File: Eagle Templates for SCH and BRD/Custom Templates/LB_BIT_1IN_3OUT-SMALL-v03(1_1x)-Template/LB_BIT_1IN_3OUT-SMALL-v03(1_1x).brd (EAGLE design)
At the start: 74.2 x 11.6 mm, 16 parts, among them U1 LV321SOT23-5

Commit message: added bitlab logo and made minor changes to board templates. Updated littlebits library.
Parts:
- added U$2: (no value), LITTLEBITS:BITLAB-LOGO
- moved U$8 4.30 mm to (67.3, 9.33)
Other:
- board text added: "iX Name Here"
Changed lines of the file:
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@@
 <layer number="113" name="extra" color="10" fill="1" visible="yes" active="yes"/>
 <layer number="116" name="Patch_BOT" color="7" fill="1" visible="yes" active="yes"/>
+<layer number="118" name="Rect_Pads" color="7" fill="1" visible="no" active="yes"/>
 <layer number="121" name="_tsilk" color="7" fill="1" visible="yes" active="yes"/>
 <layer number="122" name="_bsilk" color="7" fill="1" visible="yes" active="yes"/>
@@
 <wire x1="2.51" y1="12.705" x2="5.51" y2="15.705" width="1" layer="46" curve="-90"/>
 <wire x1="2.51" y1="4.11" x2="3.39" y2="4.11" width="1" layer="46"/>
+<text x="72.9" y="9.7" size="1.3" layer="21" font="vector" rot="SR270" align="center">iX Name
+Here</text>
 </plain>
 <attributes>
@@
 </autorouter>
 <elements>
-<element name="U$8" library="ohw-logo" package="OSHW_FILLX150_NOTEXT" value="" x="71.633" y="9.428"/>
+<element name="U$8" library="ohw-logo" package="OSHW_FILLX150_NOTEXT" value="" x="67.333" y="9.328"/>
 <element name="U1" library="LITTLEBITS" package="SOT23-5" value="LV321SOT23-5" x="42.125" y="10.465" rot="MR270"/>
 <element name="I?R1" library="LITTLEBITS" package="RES-0603" value="1meg" x="39.58" y="13.16" rot="MR180">
@@
 <element name="U$1" library="LITTLEBITS" package="OSHWCREDIT" value="OSHWCREDIT" x="-88.27" y="-63.05"/>
 <element name="FRAME1" library="LITTLEBITS" package="FABDWG01-OHW" value="FRAME-LETTER" x="0" y="0"/>
+<element name="U$2" library="LITTLEBITS" package="BITLAB-LOGO" value="" x="72" y="13.6" rot="R270"/>
 </elements>
 <signals>

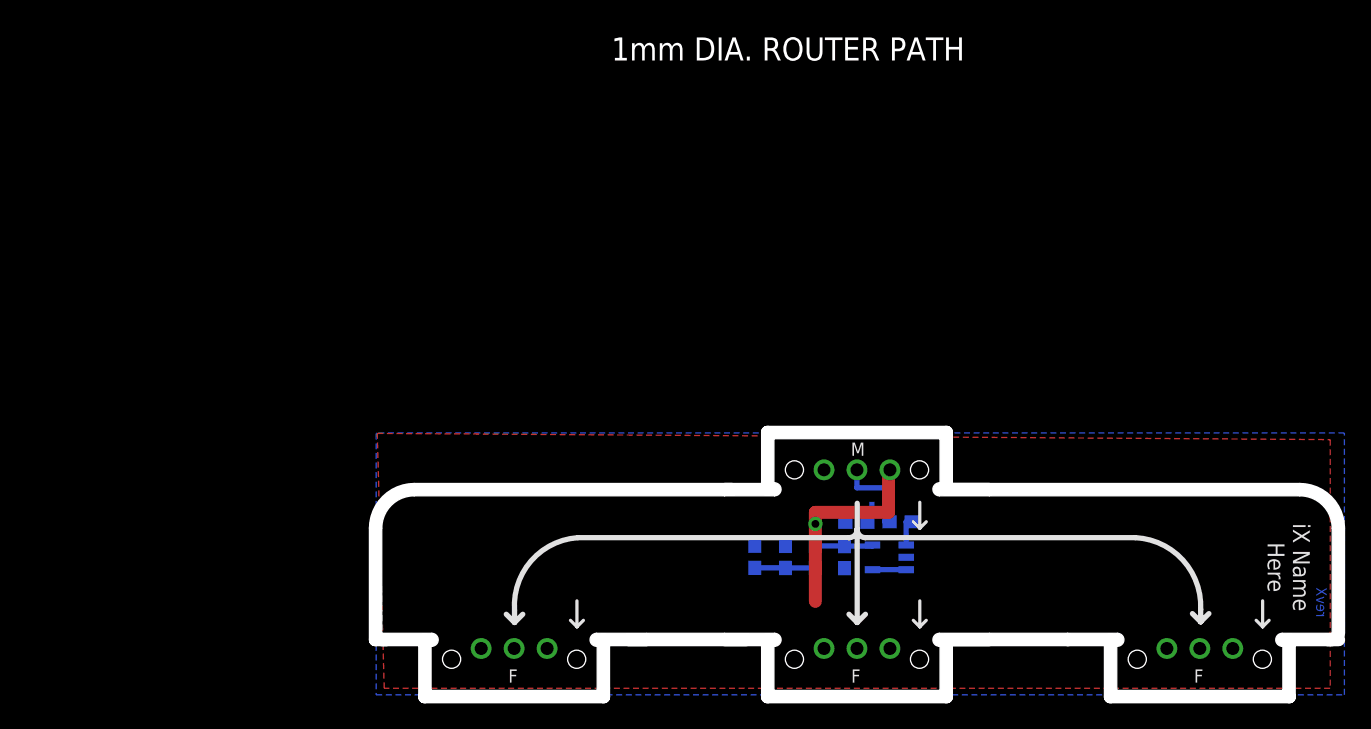
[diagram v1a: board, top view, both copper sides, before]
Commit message: Updated templates
- Added ferrite beads
- Moved text and annotations off of Nets layer
- Minor layout changes
- Removed I/O/W prefix from reference designators
- Removed output stage components from output bits
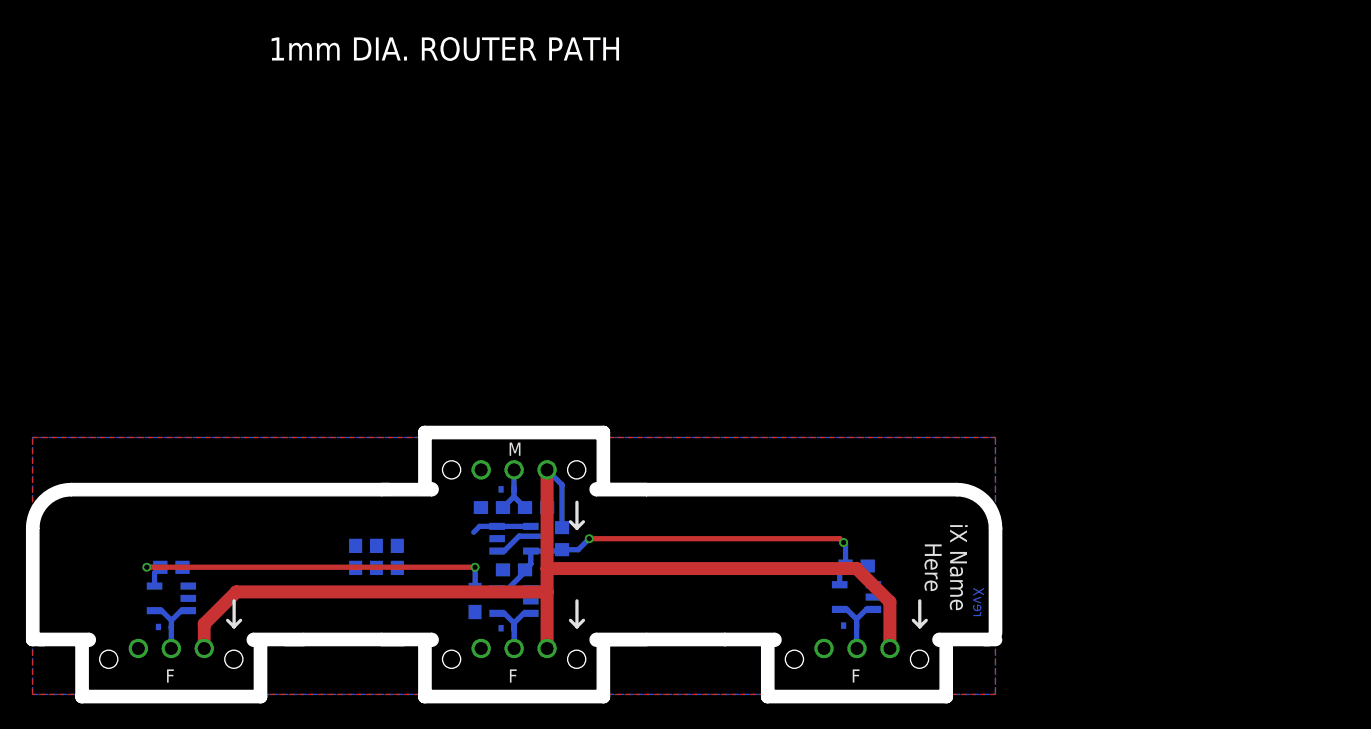
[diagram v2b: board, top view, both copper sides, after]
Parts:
- removed I?BSF2: BITSNAP_V03_FEMALE, bitSnap:BITSNAP_V03_FEMALE
- removed I?C1: 0.1uF, LITTLEBITS:CAP-0603
- removed I?C2: 10uF, LITTLEBITS:CAP-0603
- removed I?R1: 1meg, LITTLEBITS:RES-0603
- removed I?R2: 10K, LITTLEBITS:RES-0603
- removed I?R3, I?R4: 3K3, LITTLEBITS:RES-0603
- removed I?TVS1: ESD9B5.0ST5G, LITTLEBITS:SOD-923
- added BSF1: BITSNAP_V03_FEMALE, bitSnap:BITSNAP_V03_FEMALE
- added C1: 0.1uF, LITTLEBITS:CAP-0603
- added C2: 10uF, LITTLEBITS:CAP-0603
- added C3, C4, C5: 1.0uF, LITTLEBITS:CAP-0603
- added FB1: FERRITE-BEAD0603, LITTLEBITS:R0603
- added R1: 1meg, LITTLEBITS:RES-0603
- added R2: 10K, LITTLEBITS:RES-0603
- added R3, R4: 3K3, LITTLEBITS:RES-0603
- added TVS1, TVS2, TVS3, TVS4: ESD9B5.0ST5G, LITTLEBITS:SOD-923
- added U2, U3, U4: LV321SOT23-5, LITTLEBITS:SOT23-5
- moved U1 29.0 mm to (13.2, 11.9), turned to 90 degrees
- moved U$2 26.4 mm to (45.6, 13.6)
- moved U$8 26.4 mm to (40.9, 9.33)
- moved I?BSM 26.4 mm to (19.8, 19.8)
- renumbered I?BSF to BSF2, I?BSF1 to BSF3
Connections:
- new net LB_VCC: BSF1.VCC, BSF2.VCC, BSF3.VCC, FB1.2, I?BSM.VCC1
- new net N$12: U4.1
- new net N$2: U2.1
- new net N$5: U3.1
- new net SIG_OUT1: BSF1.SIG, TVS4.2, U4.3, U4.4
- new net SIG_OUT2: BSF2.SIG, TVS2.2, U2.3, U2.4
- new net SIG_OUT3: BSF3.SIG, TVS3.2, U3.3, U3.4
- net GND: now also BSF1.GND, C1.2, C2.2, C3.1, C4.1, C5.1, R1.1, R4.1, TVS1.1, TVS2.1, TVS3.1, TVS4.1, U2.2, U3.2, U4.2; no longer I?BSF2.GND, I?C1.2, I?C2.2, I?R1.1, I?R4.1, I?TVS1.1
- net N$4: now also R2.1; no longer I?R2.1
- net SIG_OUT: now also R1.2, R2.2, TVS1.2; no longer BSF2.SIG, BSF3.SIG, I?BSF2.SIG, I?R1.2, I?R2.2, I?TVS1.2
- net VCC: now also C1.1, C3.2, C4.2, C5.2, FB1.1, R3.2, U2.5, U3.5, U4.5; no longer BSF2.VCC, BSF3.VCC, I?BSF2.VCC, I?BSM.VCC1, I?C1.1, I?R3.2
- net VREF: now also C2.1, R3.1, R4.2; no longer I?C2.1, I?R3.1, I?R4.2
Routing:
- net LB_VCC: track 0.00 -> 79.1 mm
- net VCC: track 22.1 -> 64.1 mm, vias 1 -> 4
- net SIG_OUT3: track 0.00 -> 5.49 mm
- net SIG_OUT1: track 0.00 -> 5.39 mm
- net SIG_OUT2: track 0.00 -> 5.19 mm
- net VREF: track 4.68 -> 0.00 mm
- net N$4: track 2.21 -> 6.32 mm
- net SIG_OUT: track 6.53 -> 4.47 mm
- net N$3: track 2.60 -> 4.59 mm
- added copper zone on layer 16, net GND
- removed copper zone on layer 16, net N$1
